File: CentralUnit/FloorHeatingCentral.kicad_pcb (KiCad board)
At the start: 2 copper layers, 100 x 100 mm, 102 parts, among them J1 Conn_01x03, J10 Conn_01x02, J11 Conn_01x02, J12 Conn_01x02, J13 Conn_01x02, J14 Conn_01x02, J15 Conn_01x03, J16 Conn_01x03, J17 Conn_01x03, J18 Conn_01x03, J19 Conn_01x03, J2 Conn_01x03, J20 Conn_01x03, J21 Conn_01x03, J22 Conn_01x03, J23 Conn_01x03, J24 Conn_01x03, J25 Conn_02x05_Odd_Even, J26 Conn_01x02, J3 Conn_01x19, J4 Conn_01x06, J5 Conn_01x02, J6 Conn_01x02, J7 Conn_01x02, J8 Conn_01x02, J9 Conn_01x02, Q1 Q_NMOS_GDS, Q10 Q_NMOS_GDS, Q2 Q_NMOS_GDS, Q3 Q_NMOS_GDS, Q4 Q_NMOS_GDS, Q5 Q_NMOS_GDS, Q6 Q_NMOS_GDS, Q7 Q_NMOS_GDS, Q8 Q_NMOS_GDS, Q9 Q_NMOS_GDS, U1 ESP32-WROOM, U10 LM1117-3.3, U2 ISO1540DR, U3 ISO1540DR, U4 ISO1540DR, U5 ISO1540DR, U6 ISO1540DR, U7 74HC595D_118, U8 74HC595D_118, U9 MP1584

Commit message: Some improvements
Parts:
- added H1: MountingHole, parts:PCB_DINrail_holder, F.Cu at (127.5, 100.0)
- added H2: MountingHole, parts:PCB_DINrail_holder, F.Cu at (190.0, 100.0)
- added R39: 560R, Resistors_SMD:R_0603, F.Cu at (114.6, 75.0)
- added R40: 560R, Resistors_SMD:R_0603, F.Cu at (114.6, 80.2)
- added R41: 560R, Resistors_SMD:R_0603, F.Cu at (114.6, 85.4)
- added R42: 560R, Resistors_SMD:R_0603, F.Cu at (114.6, 90.1)
- added R43: 560R, Resistors_SMD:R_0603, F.Cu at (114.6, 95.3)
- added R44: 560R, Resistors_SMD:R_0603, F.Cu at (114.6, 101.3)
- added R45: 560R, Resistors_SMD:R_0603, F.Cu at (114.6, 106.5)
- added R46: 560R, Resistors_SMD:R_0603, F.Cu at (114.6, 111.6)
- added R47: 560R, Resistors_SMD:R_0603, F.Cu at (114.6, 116.5)
- added R48: 560R, Resistors_SMD:R_0603, F.Cu at (114.6, 121.7)
- moved C16 15.0 mm to (146.4, 95.9)
- moved C17 15.0 mm to (145.8, 85.1)
- moved U8 15.0 mm to (141.5, 99.7)
- moved U7 15.0 mm to (140.7, 88.9)
- moved C12 2.24 mm to (183.4, 140.2)
- moved C13 2.24 mm to (173.7, 140.2)
- moved C4 2.24 mm to (118.4, 140.2)
- moved C5 2.24 mm to (108.7, 140.2)
- moved R15 2.24 mm to (118.9, 137.7)
- moved R16 2.24 mm to (118.9, 136.2)
- moved R17 2.24 mm to (108.2, 137.7)
- moved R18 2.24 mm to (108.2, 136.2)
- moved R31 2.24 mm to (183.9, 137.7)
- moved R32 2.24 mm to (183.9, 136.2)
- moved R33 2.24 mm to (173.2, 137.7)
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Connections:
- Q1 pad 1: /ActuatorConn/GATE -> Net-(Q1-Pad1)
- Q10 pad 1: /sheet5C0169FE/GATE -> Net-(Q10-Pad1)
- Q2 pad 1: /sheet5C0162C8/GATE -> Net-(Q2-Pad1)
- Q3 pad 1: /sheet5C0163D9/GATE -> Net-(Q3-Pad1)
- Q4 pad 1: /sheet5C0163DC/GATE -> Net-(Q4-Pad1)
- Q5 pad 1: /sheet5C016537/GATE -> Net-(Q5-Pad1)
- Q6 pad 1: /sheet5C01653A/GATE -> Net-(Q6-Pad1)
- Q7 pad 1: /sheet5C01653D/GATE -> Net-(Q7-Pad1)
- Q8 pad 1: /sheet5C016540/GATE -> Net-(Q8-Pad1)
- Q9 pad 1: /sheet5C0169FB/GATE -> Net-(Q9-Pad1)
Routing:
- net /SR_LATCH: track 78.8 -> 48.8 mm
- net /SPI2CLK: track 120.9 -> 90.9 mm
- net /SPI2MOSI: track 103.4 -> 89.3 mm
- net +5V: track 281.0 -> 294.4 mm
- net /sheet5C0163DC/GATE: track 17.3 -> 29.1 mm
- net /sheet5C0162C8/GATE: track 15.6 -> 26.2 mm
- net /sheet5C0163D9/GATE: track 14.9 -> 25.2 mm
- net /sheet5C0169FB/GATE: track 41.9 -> 51.7 mm
- net /sheet5C0169FE/GATE: track 39.8 -> 49.5 mm
- net /ActuatorConn/GATE: track 23.7 -> 33.2 mm
- net /sheet5C01653D/GATE: track 28.7 -> 37.6 mm
- net /sheet5C01653A/GATE: track 24.9 -> 33.3 mm
- net /sheet5C016540/GATE: track 32.5 -> 40.9 mm
- net +3V3: track 334.6 -> 342.2 mm, vias 11 -> 12
- net /sheet5C016537/GATE: track 21.1 -> 27.3 mm
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- added copper zone on B.Cu, net GND
- added copper zone on F.Cu, net GND

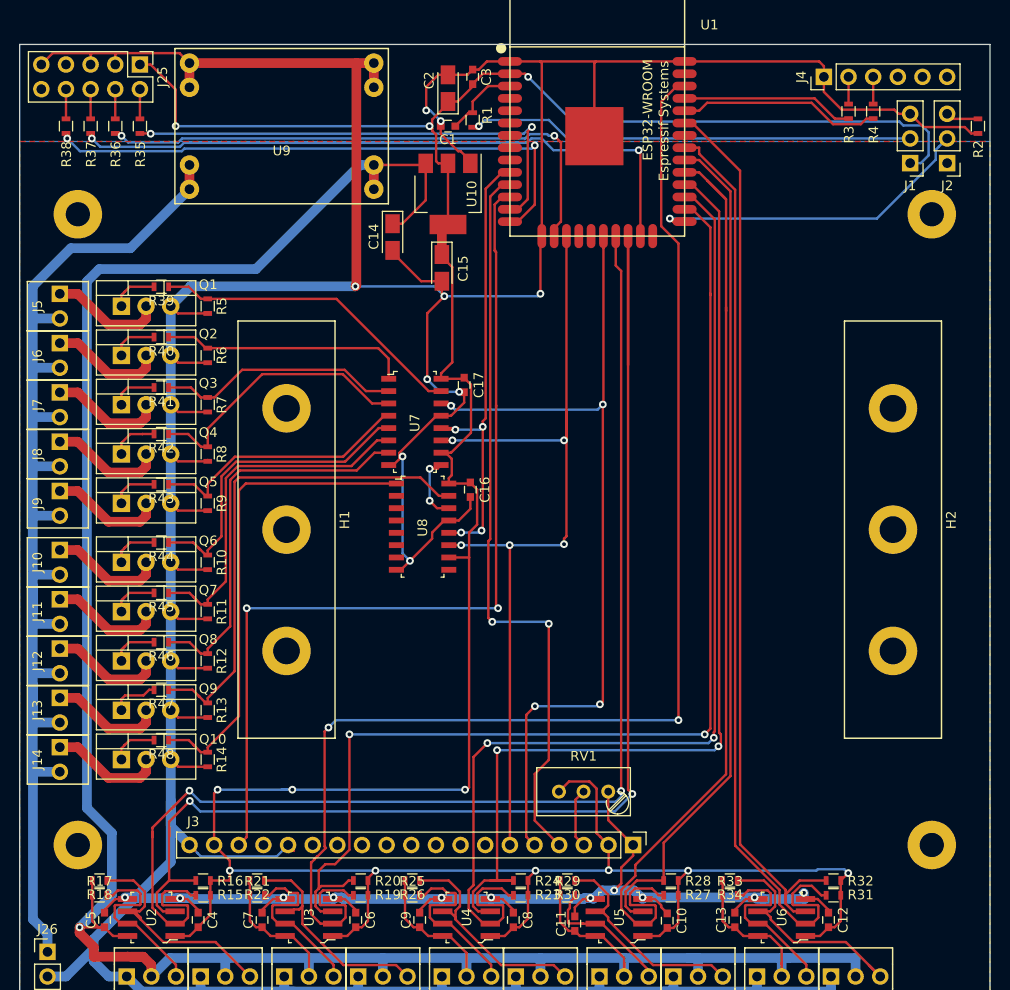
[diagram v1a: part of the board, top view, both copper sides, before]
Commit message: V2 with fixed SPI bus, status LED und changed flash header
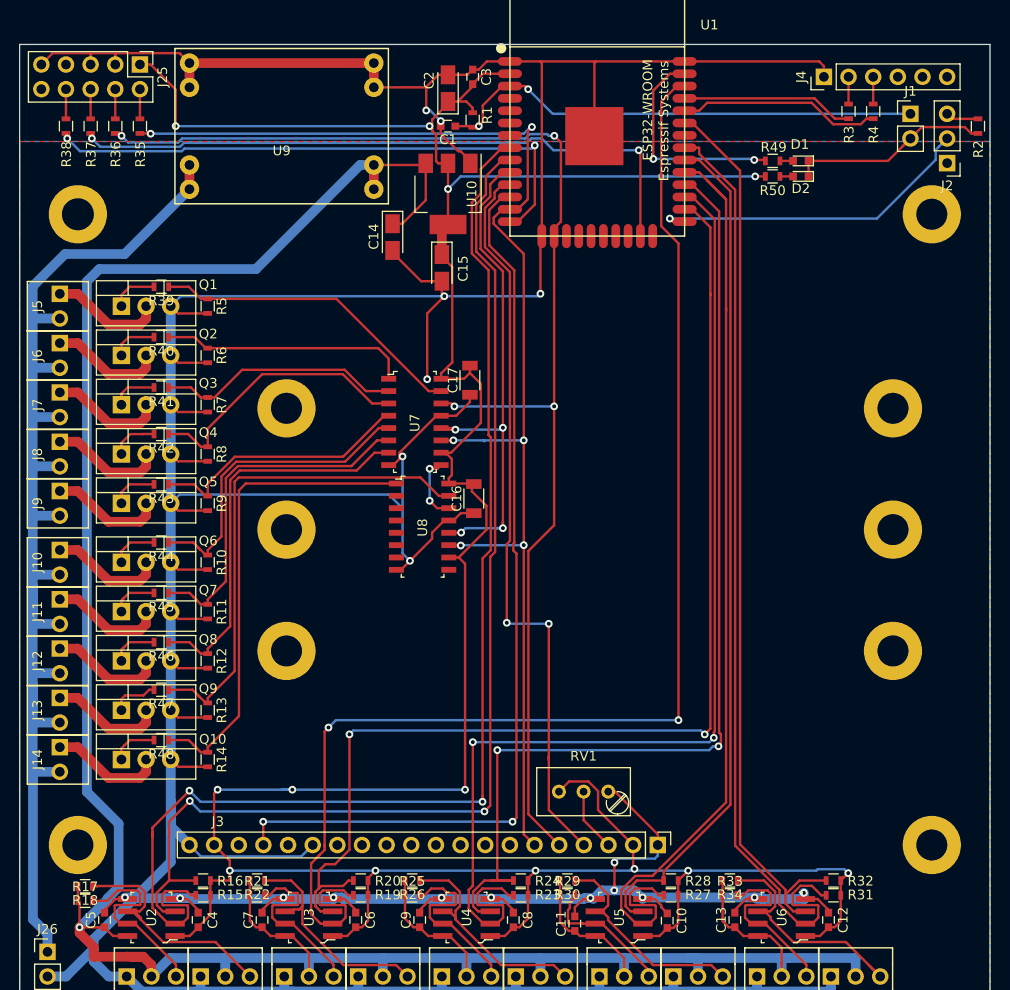
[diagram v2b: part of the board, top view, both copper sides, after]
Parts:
- added D1: LED, LEDs:LED_0603, F.Cu at (180.5, 62.0)
- added D2: LED, LEDs:LED_0603, F.Cu at (180.5, 63.6)
- added R49: 660R, Resistors_SMD:R_0603, F.Cu at (177.6, 62.0)
- added R50: 660R, Resistors_SMD:R_0603, F.Cu at (177.6, 63.6)
- C16, C17: footprint Capacitors_SMD:C_0603 -> Capacitors_SMD:C_1206
- H1, H2: moved to B.Cu
- J1: value Conn_01x03 -> Conn_01x02; footprint Pin_Headers:Pin_Header_Straight_1x03_Pitch2.54mm -> Pin_Headers:Pin_Header_Straight_1x02_Pitch2.54mm
- J3: value Conn_01x19 -> Conn_01x20
- moved J1 5.08 mm to (191.8, 57.1), turned to 0 degrees
- moved R18 1.60 mm to (106.8, 136.8)
- moved R17 1.59 mm to (106.8, 138.2)
- moved C16 0.98 mm to (146.8, 96.8)
- moved C17 0.77 mm to (146.4, 84.6)
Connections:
- net /JTAG_TDI renamed /HSPI_MISO_IO12
- net /JTAG_TDO renamed /HSPI_CS0_IO15
- J1 pad 1: +3V3 -> Net-(C1-Pad1)
- J1 pad 2: Net-(J1-Pad2) -> GND
- J3 pad 18: +3V3 -> (no net)
- J3 pad 19: GND -> +3V3
- J3 pad 5: /SPI2MOSI -> /HSPI_MOSI_IO13
- J3 pad 6: /SPI2CLK -> /HSPI_CLK_IO14
- R1 pad 1: Net-(J1-Pad2) -> Net-(C1-Pad1)
- R1 pad 2: Net-(C1-Pad1) -> +3V3
- R35 pad 1: /JTAG_TMS -> /HSPI_CLK_IO14
- R36 pad 1: /JTAG_TCK -> /HSPI_MOSI_IO13
- U1 pad 13: /JTAG_TMS -> /HSPI_CLK_IO14
- U1 pad 16: /JTAG_TCK -> /HSPI_MOSI_IO13
- U1 pad 17: /SPI2CLK -> (no net)
- U1 pad 20: /SPI2MOSI -> (no net)
- U1 pad 21: /INP0 -> (no net)
- U1 pad 22: /INP1 -> (no net)
- U1 pad 37: (no net) -> /LED
- U1 pad 8: (no net) -> /INP0
- U1 pad 9: (no net) -> /INP1
- U7 pad 11: /SPI2CLK -> /HSPI_CLK_IO14
- U7 pad 14: /SPI2MOSI -> /HSPI_MOSI_IO13
- U8 pad 11: /SPI2CLK -> /HSPI_CLK_IO14
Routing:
- net /HSPI_CLK_IO14: track 0.00 -> 135.4 mm, vias 0 -> 6
- net /HSPI_MOSI_IO13: track 0.00 -> 133.9 mm, vias 0 -> 4
- net /SPI2CLK: track 90.9 -> 0.00 mm, vias 5 -> 0
- net /SPI2MOSI: track 89.3 -> 0.00 mm, vias 4 -> 0
- net /JTAG_TCK: track 57.0 -> 0.00 mm, vias 2 -> 0
- net /JTAG_TMS: track 50.6 -> 0.00 mm, vias 2 -> 0
- net Net-(J1-Pad2): track 46.2 -> 0.00 mm, vias 1 -> 0
- net Net-(C1-Pad1): track 8.02 -> 50.9 mm, vias 0 -> 2
- net /LED: track 0.00 -> 22.6 mm, vias 0 -> 2
- net /INP1: track 135.7 -> 119.1 mm
- net +3V3: track 342.2 -> 331.7 mm, vias 12 -> 13
- net GND: track 619.7 -> 629.9 mm, vias 20 -> 19
- net /SR_LATCH: track 48.8 -> 54.5 mm
- net /INP0: track 131.0 -> 129.1 mm
- net Net-(J15-Pad3): track 19.2 -> 21.0 mm
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
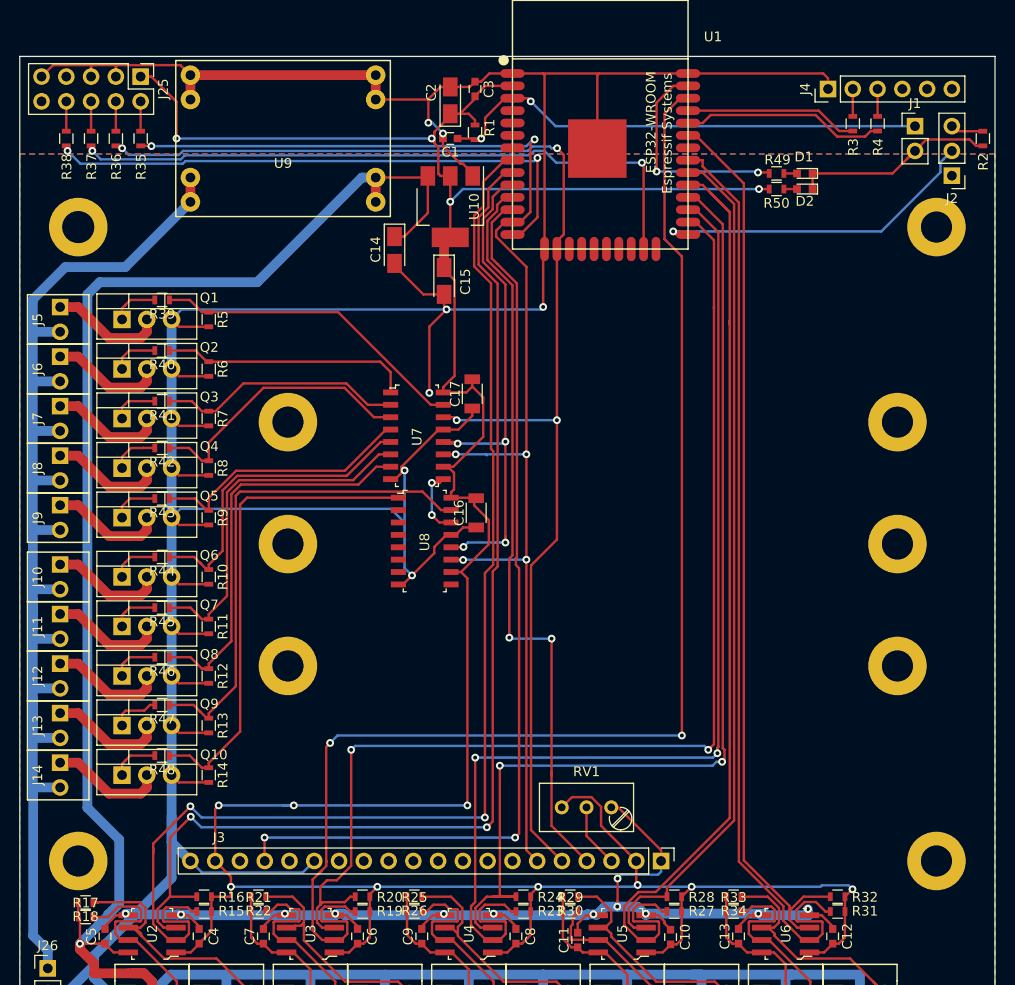
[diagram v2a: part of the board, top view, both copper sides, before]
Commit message: Bugfixes: Wrong use of GPIO15, removed header for GPIO2
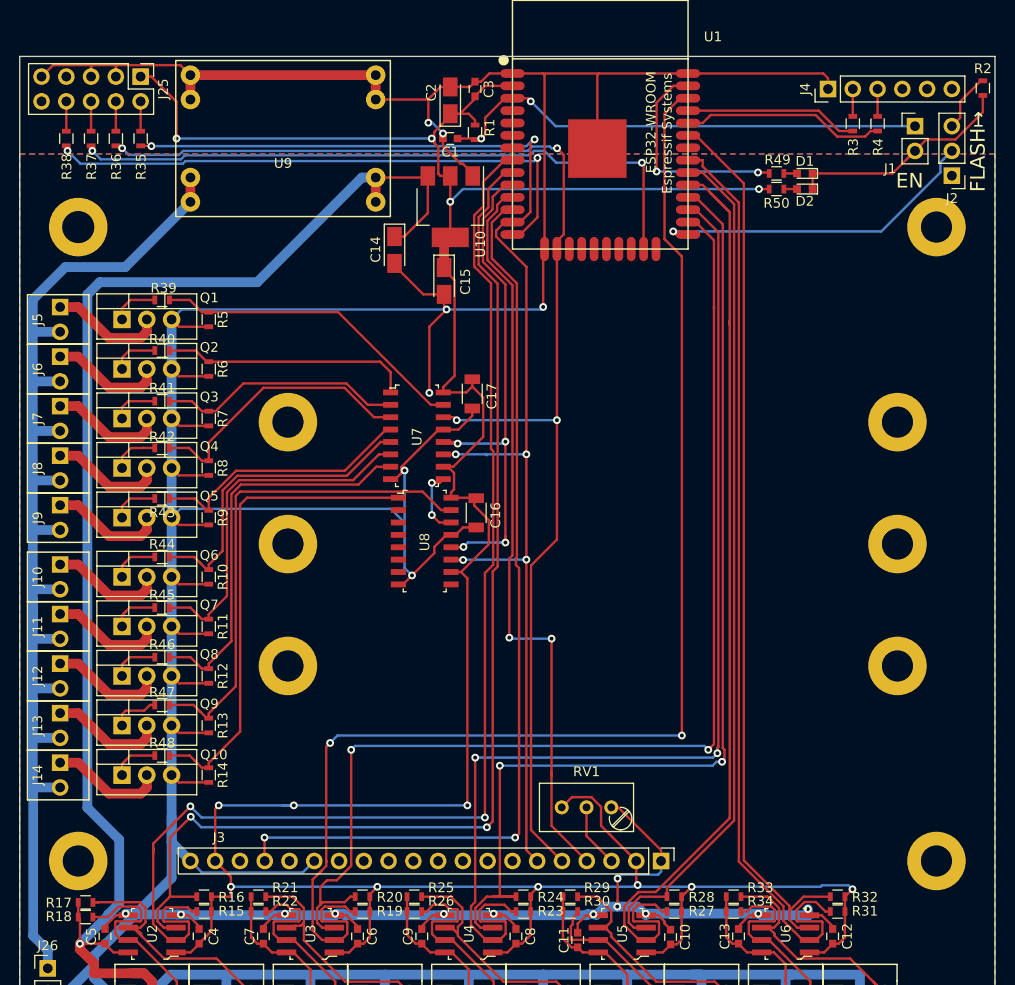
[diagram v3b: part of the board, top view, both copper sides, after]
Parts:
- moved R2 5.17 mm to (198.8, 53.2)
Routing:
- net Net-(J2-Pad3): track 3.39 -> 6.82 mm
- net GND: track 629.9 -> 632.5 mm
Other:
- board text added: "EN"
- board text added: "FLASH↦"
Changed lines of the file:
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@@
   (general
     (thickness 1.6)
-    (drawings 4)
-    (tracks 1300)
+    (drawings 6)
+    (tracks 1304)
     (zones 0)
     (modules 118)
@@
     (descr "Through hole straight pin header, 1x02, 2.54mm pitch, single row")
     (tags "Through hole pin header THT 1x02 2.54mm single row")
-    (fp_text reference J1 (at 0 -2.33) (layer F.SilkS)
+    (fp_text reference J1 (at -2.55 4.35) (layer F.SilkS)
       (effects (font (size 1 1) (thickness 0.15)))
     )
@@
     (tags "LED led 0603 SMD smd SMT smt smdled SMDLED smtled SMTLED")
     (attr smd)
-    (fp_text reference D1 (at 0.1 1.7 180) (layer F.SilkS)
+    (fp_text reference D1 (at 0 1.25 180) (layer F.SilkS)
       (effects (font (size 1 1) (thickness 0.15)))
     )
@@
     (tags "resistor 0603")
     (attr smd)
-    (fp_text reference R48 (at 0 -1.45 180) (layer F.SilkS)
+    (fp_text reference R48 (at 0 1.3 180) (layer F.SilkS)
       (effects (font (size 1 1) (thickness 0.15)))
     )
@@
     (tags "resistor 0603")
     (attr smd)
-    (fp_text reference R47 (at 0 -1.45 180) (layer F.SilkS)
+    (fp_text reference R47 (at 0 1.3 180) (layer F.SilkS)
       (effects (font (size 1 1) (thickness 0.15)))
     )
@@
     (tags "resistor 0603")
     (attr smd)
-    (fp_text reference R46 (at 0 -1.45 180) (layer F.SilkS)
+    (fp_text reference R46 (at 0 1.3 180) (layer F.SilkS)
       (effects (font (size 1 1) (thickness 0.15)))
     )
@@
     (tags "resistor 0603")
     (attr smd)
-    (fp_text reference R45 (at 0 -1.45 180) (layer F.SilkS)
+    (fp_text reference R45 (at 0 1.3 180) (layer F.SilkS)
       (effects (font (size 1 1) (thickness 0.15)))
     )
@@
     (tags "resistor 0603")
     (attr smd)
-    (fp_text reference R44 (at 0 -1.45 180) (layer F.SilkS)
+    (fp_text reference R44 (at 0 1.3 180) (layer F.SilkS)
       (effects (font (size 1 1) (thickness 0.15)))
     )
@@
     (tags "resistor 0603")
     (attr smd)
-    (fp_text reference R42 (at 0 -1.45 180) (layer F.SilkS)
+    (fp_text reference R42 (at 0 1.143333 180) (layer F.SilkS)
       (effects (font (size 1 1) (thickness 0.15)))
     )
@@
     (tags "resistor 0603")
     (attr smd)
-    (fp_text reference R41 (at 0 -1.45 180) (layer F.SilkS)
+    (fp_text reference R41 (at 0 1.352222 180) (layer F.SilkS)
       (effects (font (size 1 1) (thickness 0.15)))
     )
@@
     (tags "resistor 0603")
     (attr smd)
-    (fp_text reference R40 (at 0 -1.45 180) (layer F.SilkS)
+    (fp_text reference R40 (at 0 1.161111 180) (layer F.SilkS)
       (effects (font (size 1 1) (thickness 0.15)))
     )
@@
     (tags "resistor 0603")
     (attr smd)
-    (fp_text reference R39 (at 0 -1.45 180) (layer F.SilkS)
+    (fp_text reference R39 (at -0.15 1.22 180) (layer F.SilkS)
       (effects (font (size 1 1) (thickness 0.15)))
     )
@@
     (tags "CMS SOT")
     (attr smd)
-    (fp_text reference U10 (at -0.005 -2.455 270) (layer F.SilkS)
+    (fp_text reference U10 (at 3.845 -3.105 270) (layer F.SilkS)
       (effects (font (size 1 1) (thickness 0.15)))
     )
@@
   )
   (module Resistors_SMD:R_0603 (layer F.Cu)
-    (at 198.755 58.42 90)
+    (at 198.755 53.25 90)
     (descr "Resistor SMD 0603, reflow soldering, Vishay (see dcrcw.pdf)")
     (tags "resistor 0603")
     (attr smd)
-    (fp_text reference R2 (at -2.38 0.045 90) (layer F.SilkS)
+    (fp_text reference R2 (at 2 -0.005 180) (layer F.SilkS)
       (effects (font (size 1 1) (thickness 0.15)))
     )
@@
     (tags "resistor 0603")
     (attr smd)
-    (fp_text reference R17 (at 0 -1.45) (layer F.SilkS)
+    (fp_text reference R17 (at -2.75 -1.45) (layer F.SilkS)
       (effects (font (size 1 1) (thickness 0.15)))
     )
@@
     (tags "resistor 0603")
     (attr smd)
-    (fp_text reference R18 (at 0 -1.45 180) (layer F.SilkS)
+    (fp_text reference R18 (at 2.75 -1.45 180) (layer F.SilkS)
       (effects (font (size 1 1) (thickness 0.15)))
     )
@@
     (tags "resistor 0603")
     (attr smd)
-    (fp_text reference R21 (at 0 -1.45) (layer F.SilkS)
+    (fp_text reference R21 (at 2.75 -2.45) (layer F.SilkS)
       (effects (font (size 1 1) (thickness 0.15)))
     )
@@
     (tags "resistor 0603")
     (attr smd)
-    (fp_text reference R22 (at 0 -1.45 180) (layer F.SilkS)
+    (fp_text reference R22 (at -2.75 -0.45 180) (layer F.SilkS)
       (effects (font (size 1 1) (thickness 0.15)))
     )
@@
     (tags "resistor 0603")
     (attr smd)
-    (fp_text reference R25 (at 0 -1.45) (layer F.SilkS)
+    (fp_text reference R25 (at 2.75 -2.45) (layer F.SilkS)
       (effects (font (size 1 1) (thickness 0.15)))
     )
@@
     (tags "resistor 0603")
     (attr smd)
-    (fp_text reference R26 (at 0 -1.45 180) (layer F.SilkS)
+    (fp_text reference R26 (at -2.75 -0.45 180) (layer F.SilkS)
       (effects (font (size 1 1) (thickness 0.15)))
     )
@@
     (tags "resistor 0603")
     (attr smd)
-    (fp_text reference R29 (at 0 -1.45) (layer F.SilkS)
+    (fp_text reference R29 (at 2.75 -2.45) (layer F.SilkS)
       (effects (font (size 1 1) (thickness 0.15)))
     )
@@
     (tags "resistor 0603")
     (attr smd)
-    (fp_text reference R30 (at 0 -1.45 180) (layer F.SilkS)
+    (fp_text reference R30 (at -2.75 -0.45 180) (layer F.SilkS)
       (effects (font (size 1 1) (thickness 0.15)))
     )
@@
     (tags "resistor 0603")
     (attr smd)
-    (fp_text reference R33 (at 0 -1.45) (layer F.SilkS)
+    (fp_text reference R33 (at 2.75 -2.45) (layer F.SilkS)
       (effects (font (size 1 1) (thickness 0.15)))
     )
@@
     (tags "resistor 0603")
     (attr smd)
-    (fp_text reference R34 (at 0 -1.45 180) (layer F.SilkS)
+    (fp_text reference R34 (at -2.75 -0.45 180) (layer F.SilkS)
       (effects (font (size 1 1) (thickness 0.15)))
     )
@@
     (tags "capacitor 1206")
     (attr smd)
-    (fp_text reference C16 (at 0 -1.75 90) (layer F.SilkS)
+    (fp_text reference C16 (at -0.25 2 90) (layer F.SilkS)
       (effects (font (size 1 1) (thickness 0.15)))
     )
@@
     (tags "capacitor 1206")
     (attr smd)
-    (fp_text reference C17 (at 0 -1.75 90) (layer F.SilkS)
+    (fp_text reference C17 (at -0.25 2 90) (layer F.SilkS)
       (effects (font (size 1 1) (thickness 0.15)))
     )
@@
     )
   )
+  (gr_text FLASH↦ (at 198.25 59.75 90) (layer F.SilkS)
+    (effects (font (size 1.5 1.5) (thickness 0.3)))
+  )
+  (gr_text EN (at 191.25 62.75) (layer F.SilkS)
+    (effects (font (size 1.5 1.5) (thickness 0.3)))
+  )
   (gr_line (start 100 150) (end 100 50) (layer Edge.Cuts) (width 0.05))
   (gr_line (start 200 150) (end 100 150) (layer Edge.Cuts) (width 0.05))
@@
   (segment (start 161.3 134.3) (end 161.699999 133.900001) (width 0.25) (layer B.Cu) (net 2))
   (segment (start 190.950001 60.539999) (end 191.8 59.69) (width 0.25) (layer F.Cu) (net 2) (status 30))
-  (segment (start 198.055 59.17) (end 198.755 59.17) (width 0.25) (layer F.Cu) (net 2) (status 20))
-  (segment (start 197.399999 58.514999) (end 198.055 59.17) (width 0.25) (layer F.Cu) (net 2))
-  (segment (start 192.975001 58.514999) (end 197.399999 58.514999) (width 0.25) (layer F.Cu) (net 2))
   (segment (start 191.8 59.69) (end 192.975001 58.514999) (width 0.25) (layer F.Cu) (net 2) (status 10))
   (segment (start 189.49 62) (end 191.8 59.69) (width 0.25) (layer F.Cu) (net 2) (status 20))
@@
   (segment (start 116.594 75.946) (end 143.764 75.946) (width 0.25) (layer B.Cu) (net 2))
   (segment (start 115.57 76.97) (end 116.594 75.946) (width 0.25) (layer B.Cu) (net 2) (status 10))
+  (segment (start 198.755 55.714002) (end 198.755 54.5) (width 0.25) (layer F.Cu) (net 2))
+  (segment (start 198.755 54.5) (end 198.755 54) (width 0.25) (layer F.Cu) (net 2))
+  (segment (start 195.954003 58.514999) (end 198.755 55.714002) (width 0.25) (layer F.Cu) (net 2))
+  (segment (start 192.975001 58.514999) (end 195.954003 58.514999) (width 0.25) (layer F.Cu) (net 2))
   (segment (start 163.195 132.525794) (end 163.22 132.500794) (width 0.25) (layer F.Cu) (net 3) (status 30))
   (segment (start 163.195 132.525794) (end 163.22 132.500794) (width 0.25) (layer B.Cu) (net 3) (status 30))
@@
   (segment (start 167.005 67.945) (end 188.340002 67.945) (width 0.25) (layer B.Cu) (net 4))
   (segment (start 196.1 57.67) (end 195.58 57.15) (width 0.25) (layer F.Cu) (net 5) (status 30))
-  (segment (start 198.755 57.67) (end 196.1 57.67) (width 0.25) (layer F.Cu) (net 5) (status 30))
+  (segment (start 196.429999 56.300001) (end 196.429999 54.625001) (width 0.25) (layer F.Cu) (net 5))
+  (segment (start 198.555 52.5) (end 198.755 52.5) (width 0.25) (layer F.Cu) (net 5))
+  (segment (start 196.429999 54.625001) (end 198.555 52.5) (width 0.25) (layer F.Cu) (net 5))
+  (segment (start 195.58 57.15) (end 196.429999 56.300001) (width 0.25) (layer F.Cu) (net 5))
   (via (at 150.8 130.1) (size 0.8) (drill 0.4) (layers F.Cu B.Cu) (net 6))
   (via (at 125.1 130.1) (size 0.8) (drill 0.4) (layers F.Cu B.Cu) (net 6))
